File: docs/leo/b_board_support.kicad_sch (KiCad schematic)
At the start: 9 parts, among them IC19 74LS175, IC20 74LS32, IC21 74LS74, IC22 74LS32, IC28 74LS138, IC29 74LS74, IC35 74LS175, IC36 74LS157, J20 Jumper_3_Bridged12

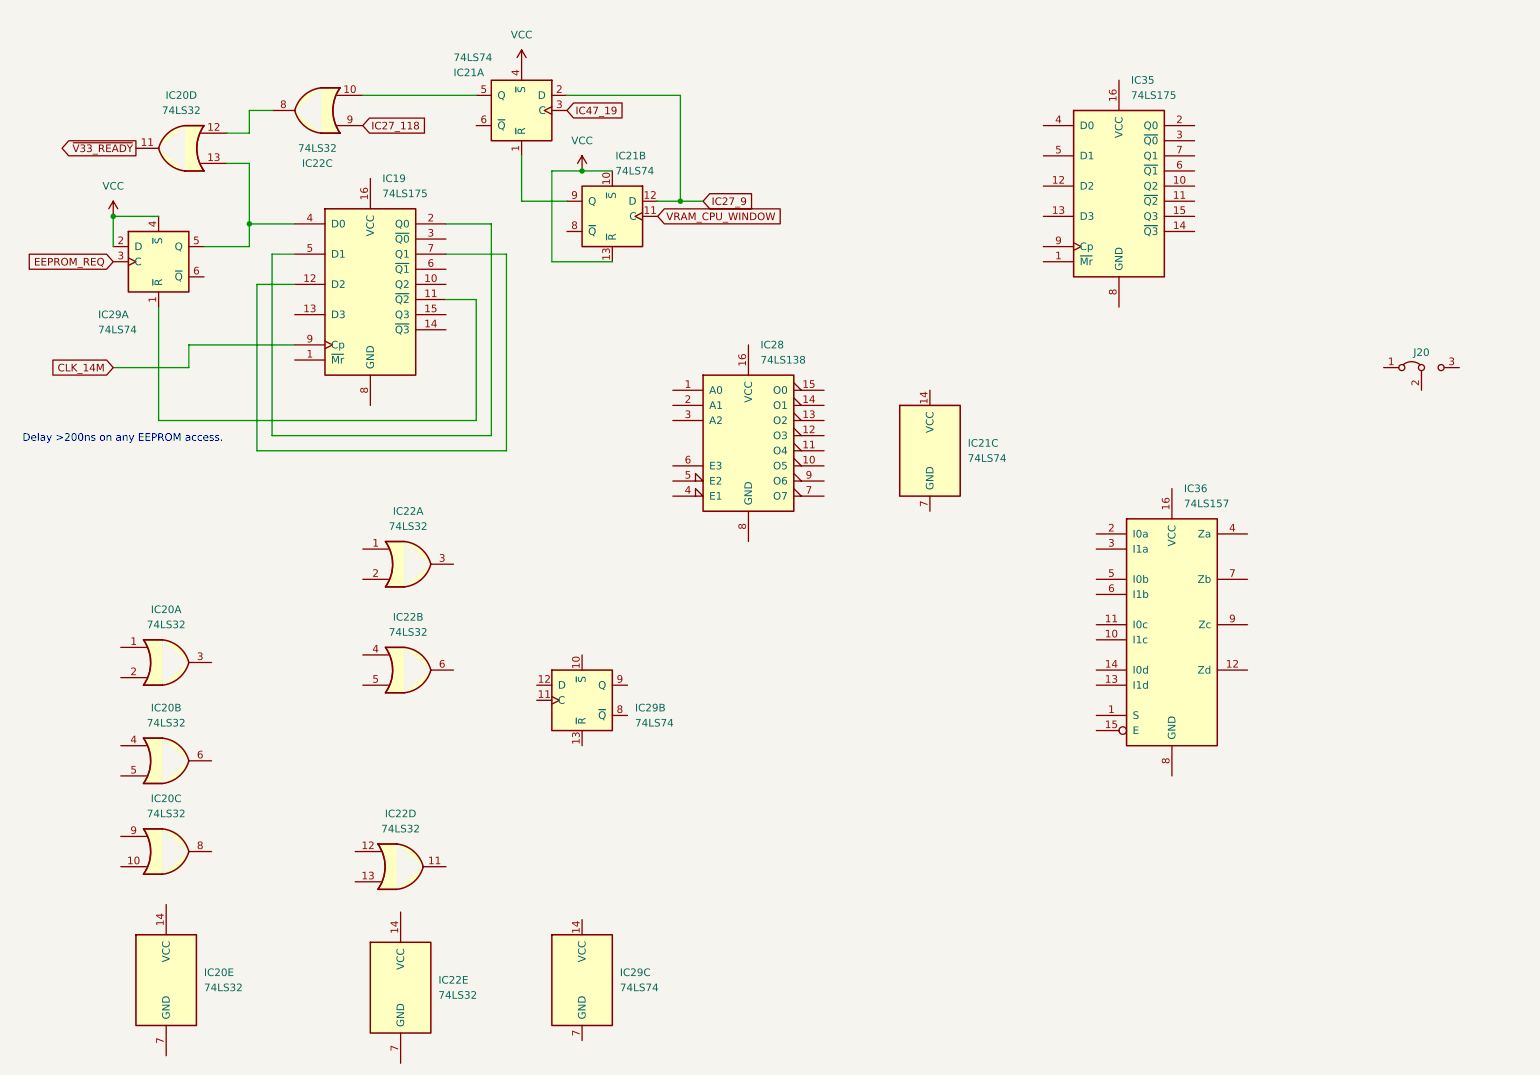
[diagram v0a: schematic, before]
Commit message: Split bank switching into its own sheet
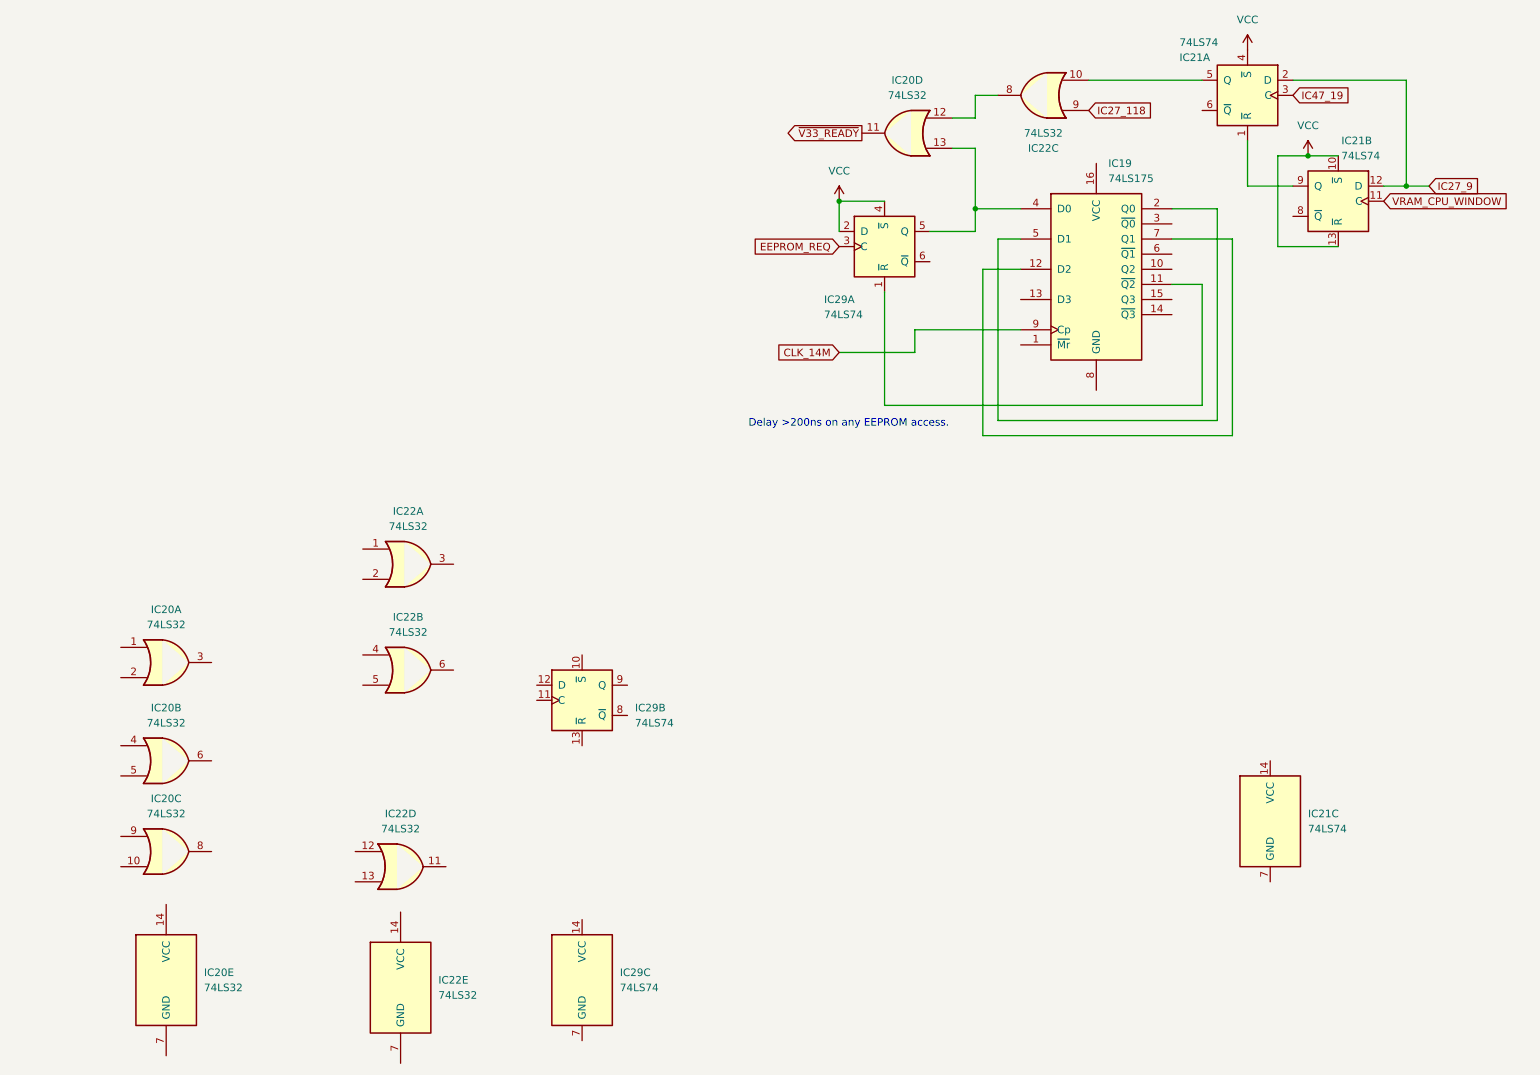
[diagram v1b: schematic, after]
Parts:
- removed IC28: 74LS138, symbol 74xx:74LS138
- removed IC35: 74LS175, symbol 74xx:74LS175
- removed IC36: 74LS157, symbol 74xx:74LS157
- removed J20: Jumper_3_Bridged12, symbol Jumper:Jumper_3_Bridged12
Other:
- moved on the sheet: IC19, IC20D, IC21A, IC21B, IC21C, IC22C, IC29A

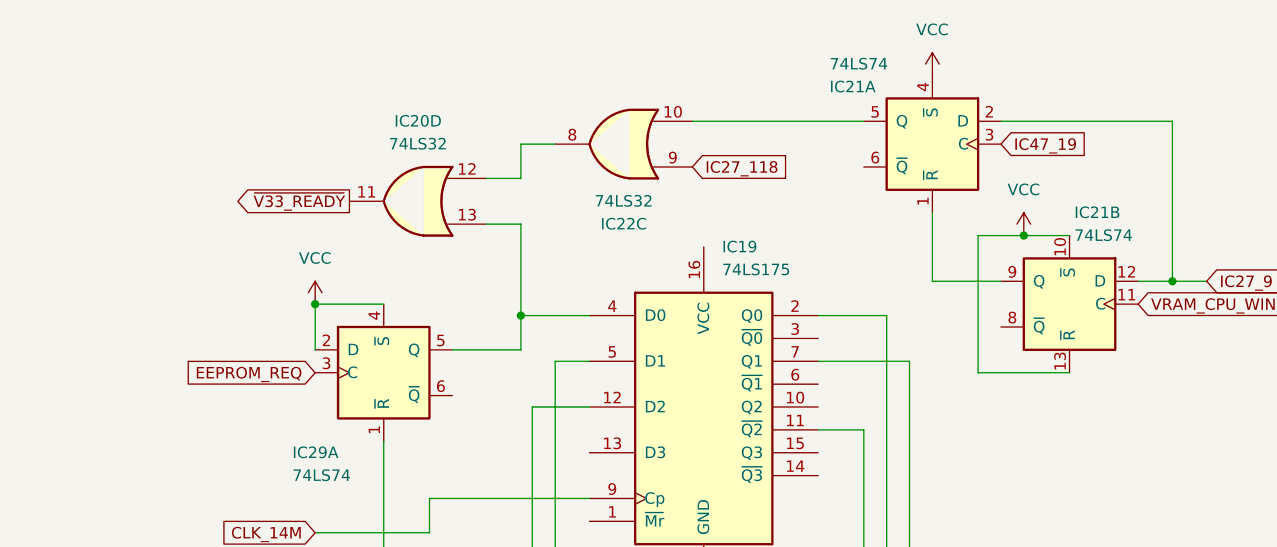
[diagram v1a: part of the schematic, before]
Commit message: Decode M92-B-7H-D PAL
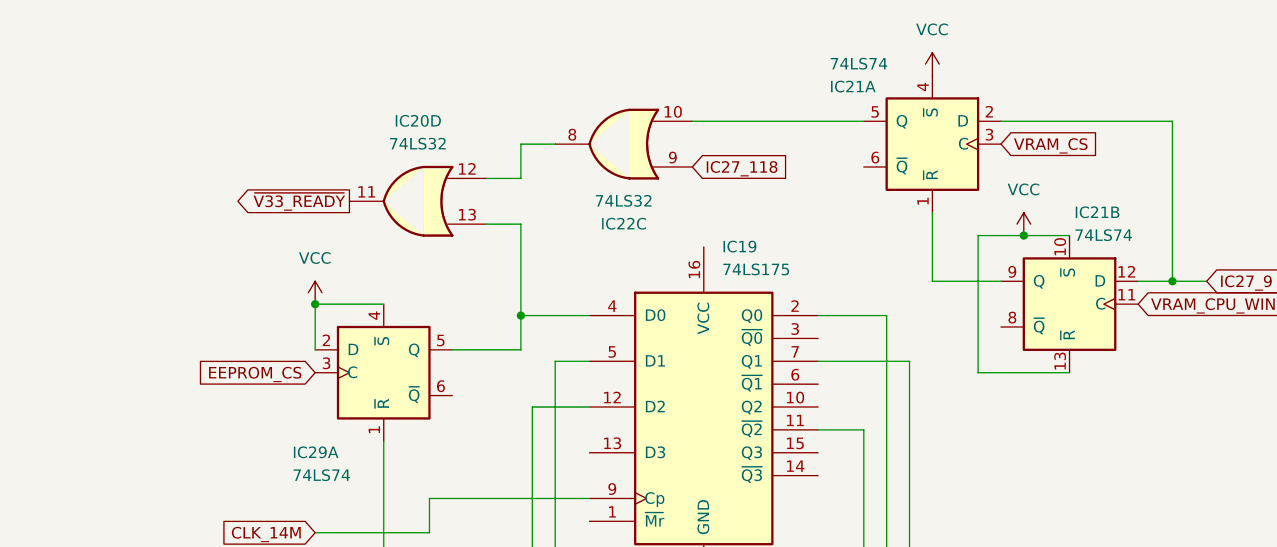
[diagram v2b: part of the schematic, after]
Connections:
- net EEPROM_REQ renamed EEPROM_CS
- net IC47_19 renamed VRAM_CS
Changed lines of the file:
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@@
     )
   )
-  (global_label "EEPROM_REQ" (shape input) (at 156.21 55.88 180) (fields_autoplaced)
+  (global_label "EEPROM_CS" (shape input) (at 156.21 55.88 180) (fields_autoplaced)
     (effects (font (size 1.27 1.27)) (justify right))
-    (property "Intersheet References" "${INTERSHEET_REFS}" (id 0) (at 141.4598 55.8006 0)
+    (property "Intersheet References" "${INTERSHEET_REFS}" (id 0) (at 142.7298 55.8006 0)
       (effects (font (size 1.27 1.27)) (justify right) hide)
     )
@@
     )
   )
-  (global_label "IC47_19" (shape input) (at 232.41 30.48 0) (fields_autoplaced)
+  (global_label "VRAM_CS" (shape input) (at 232.41 30.48 0) (fields_autoplaced)
     (effects (font (size 1.27 1.27)) (justify left))
-    (property "Intersheet References" "${INTERSHEET_REFS}" (id 0) (at 242.5036 30.4006 0)
+    (property "Intersheet References" "${INTERSHEET_REFS}" (id 0) (at 243.1688 30.4006 0)
       (effects (font (size 1.27 1.27)) (justify left) hide)
     )
